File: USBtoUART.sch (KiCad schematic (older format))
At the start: 21 parts, among them J4 UJ2-MIBH-4-SMT-TR, U1 FT2232D-REEL, Y1 AS-6.000-12-2020-EXT-SMD-TR

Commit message: Changed J9 connections to help with layout.
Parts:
- JP4, JP5: footprint SMT-JUMPER_3_1-NC -> Jumpers:SMT-JUMPER_3_1-NC_TRACE_NO-SILK
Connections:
- net labels added: 3V3OUT, EEDATA, RESET, RSTOUT, USBDM, USBDM_IN, USBDP, USBDP_IN, XOUT, XTIN
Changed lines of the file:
@@
 Wire Wire Line
 	2600 1350 2750 1350
-Text HLabel 4450 3800 0    50   Input ~ 0
+Text HLabel 4150 3800 0    50   Input ~ 0
 GPS.TXD
-Text HLabel 4450 3900 0    50   Input ~ 0
+Text HLabel 4150 3900 0    50   Input ~ 0
 GPS.RXD
-Wire Wire Line
-	4450 3900 4650 3900
-Wire Wire Line
-	4450 3800 4650 3800
 Text HLabel 1400 4800 0    50   Input ~ 0
 UART2.RXD
@@
 F 0 "JP5" H 2104 4905 45  0000 L CNN
 F 1 "JUMPER-SMT_3_1-NC" H 2104 4989 45  0000 L CNN
-F 2 "SMT-JUMPER_3_1-NC" H 2000 5250 20  0001 C CNN
+F 2 "Jumpers:SMT-JUMPER_3_1-NC_TRACE_NO-SILK" H 2000 5250 20  0001 C CNN
 F 3 "" V 2000 4945 60  0001 C CNN
 F 4 "XXX-00000" H 2104 5084 60  0000 L CNN "PROD_ID"
@@
 AR Path="/5F7C6408/5F8DF40E" Ref="JP?"  Part="1"
 AR Path="/5F8460BD/5F8DF40E" Ref="JP4"  Part="1"
-F 0 "JP4" H 1854 5605 45  0000 L CNN
-F 1 "JUMPER-SMT_3_1-NC" H 1854 5689 45  0000 L CNN
-F 2 "SMT-JUMPER_3_1-NC" H 1750 5950 20  0001 C CNN
+F 0 "JP4" H 1854 5795 45  0000 L CNN
+F 1 "JUMPER-SMT_3_1-NC" H 1854 5711 45  0000 L CNN
+F 2 "Jumpers:SMT-JUMPER_3_1-NC_TRACE_NO-SILK" H 1750 5950 20  0001 C CNN
 F 3 "" V 1750 5645 60  0001 C CNN
-F 4 "XXX-00000" H 1854 5784 60  0000 L CNN "PROD_ID"
+F 4 "XXX-00000" H 1854 5616 60  0000 L CNN "PROD_ID"
 	1    1750 5700
 	-1   0    0    -1
@@
 	8500 3300 8500 3000
 Connection ~ 8500 3000
+Text Label 4350 2300 0    50   ~ 0
+EEDATA
+Text Label 4350 2100 0    50   ~ 0
+USBDM
+Text Label 4350 2000 0    50   ~ 0
+USBDP
+Wire Wire Line
+	4150 3800 4650 3800
+Wire Wire Line
+	4150 3900 4650 3900
+Text Label 4250 3800 0    50   ~ 0
+GPS.TXD
+Text Label 4250 3900 0    50   ~ 0
+GPS.RXD
+Text Label 3550 5000 0    50   ~ 0
+UART2.RXD
+Text Label 3550 5700 0    50   ~ 0
+UART2.TXD
+Text Label 5950 2800 0    50   ~ 0
+RSTOUT
+Text Label 5950 3000 0    50   ~ 0
+XOUT
+Text Label 5950 3100 0    50   ~ 0
+3V3OUT
+Text Label 3600 2600 0    50   ~ 0
+XTIN
+Text Label 4050 2400 0    50   ~ 0
+RESET
+Text Label 2350 2100 0    50   ~ 0
+USBDM_IN
+Text Label 2350 2000 0    50   ~ 0
+USBDP_IN
 $EndSCHEMATC

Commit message: Changed crystal for resonator. Board Layout.
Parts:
- removed C1, C2: 12pF, Capacitor_SMD:C_0805_2012Metric_Pad1.18x1.45mm_HandSolder, symbol Device:C
- removed Y1: AS-6.000-12-2020-EXT-SMD-TR, Crystal:Crystal_SMD_HC49-SD_HandSoldering, symbol Device:Crystal
- added R13: 1M, Resistor_SMD:R_0805_2012Metric_Pad1.20x1.40mm_HandSolder, symbol Device:R_US
- added Y1: CSTNR6M00GH5C000R0, LMS-6_Interface_Board:CSTNR_Resonator, symbol Device:Resonator
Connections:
- wire segments 95 -> 96
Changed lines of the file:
@@
 Title "USB to UART"
 Date "2020-10-17"
-Rev "5"
+Rev "6"
 Comp ""
 Comment1 ""
@@
 	1650 2000 2700 2000
 Wire Wire Line
-	3000 2000 4650 2000
+	3000 2000 3900 2000
 Wire Wire Line
 	1650 2100 3200 2100
@@
 Text HLabel 1400 5900 0    50   Input ~ 0
 UART2.TXD
-$Comp
-L Device:Crystal Y1
-U 1 1 5F86847C
-P 3350 3000
-F 0 "Y1" V 3304 3131 50  0000 L CNN
-F 1 "AS-6.000-12-2020-EXT-SMD-TR" V 3395 3131 50  0000 L CNN
-F 2 "Crystal:Crystal_SMD_HC49-SD_HandSoldering" H 3350 3000 50  0001 C CNN
-F 3 "http://www.raltron.com/wp-content/uploads/2016/10/crystal_as-smd.pdf" H 3350 3000 50  0001 C CNN
-F 4 "Raltron Electronics" V 3350 3000 50  0001 C CNN "Manufactuer"
-F 5 "AS-6.000-12-2020-EXT-SMD-TR" V 3350 3000 50  0001 C CNN "MPN"
-	1    3350 3000
-	0    1    1    0
-$EndComp
 Wire Wire Line
 	4650 2600 3350 2600
 Wire Wire Line
-	3350 2600 3350 2850
-Wire Wire Line
-	3350 3150 3350 3350
-Wire Wire Line
 	3350 6350 6600 6350
 Wire Wire Line
@@
 Wire Wire Line
 	6600 3000 5850 3000
-$Comp
-L Device:C C1
-U 1 1 5F869A1D
-P 2750 2800
-F 0 "C1" H 2865 2846 50  0000 L CNN
-F 1 "12pF" H 2865 2755 50  0000 L CNN
-F 2 "Capacitor_SMD:C_0805_2012Metric_Pad1.18x1.45mm_HandSolder" H 2750 2800 50  0001 C CNN
-F 3 "https://www.yageo.com/upload/media/product/productsearch/datasheet/mlcc/UPY-GP_NP0_16V-to-50V_18.pdf" H 2750 2800 50  0001 C CNN
-F 4 "Yageo" H 2750 2800 50  0001 C CNN "Manufacturer"
-F 5 "CC0805JRNPO9BN120" H 2750 2800 50  0001 C CNN "MPN"
-	1    2750 2800
-	1    0    0    -1
-$EndComp
-$Comp
-L Device:C C2
-U 1 1 5F86A608
-P 2750 3600
-F 0 "C2" H 2865 3646 50  0000 L CNN
-F 1 "12pF" H 2865 3555 50  0000 L CNN
-F 2 "Capacitor_SMD:C_0805_2012Metric_Pad1.18x1.45mm_HandSolder" H 2750 3600 50  0001 C CNN
-F 3 "https://www.yageo.com/upload/media/product/productsearch/datasheet/mlcc/UPY-GP_NP0_16V-to-50V_18.pdf" H 2750 3600 50  0001 C CNN
-F 4 "Yageo" H 2750 3600 50  0001 C CNN "Manufacturer"
-F 5 "CC0805JRNPO9BN120" H 2750 3600 50  0001 C CNN "MPN"
-	1    2750 3600
-	1    0    0    -1
-$EndComp
-$Comp
-L power:GND #PWR04
-U 1 1 5F86A976
-P 2750 3000
-F 0 "#PWR04" H 2750 2750 50  0001 C CNN
-F 1 "GND" H 2755 2827 50  0000 C CNN
-F 2 "" H 2750 3000 50  0001 C CNN
-F 3 "" H 2750 3000 50  0001 C CNN
-	1    2750 3000
-	1    0    0    -1
-$EndComp
-$Comp
-L power:GND #PWR05
-U 1 1 5F86AC39
-P 2750 3850
-F 0 "#PWR05" H 2750 3600 50  0001 C CNN
-F 1 "GND" H 2755 3677 50  0000 C CNN
-F 2 "" H 2750 3850 50  0001 C CNN
-F 3 "" H 2750 3850 50  0001 C CNN
-	1    2750 3850
-	1    0    0    -1
-$EndComp
-Wire Wire Line
-	2750 3850 2750 3750
-Wire Wire Line
-	2750 3450 2750 3350
-Wire Wire Line
-	2750 3350 3350 3350
-Connection ~ 3350 3350
-Wire Wire Line
-	3350 3350 3350 6350
-Wire Wire Line
-	2750 2650 2750 2600
-Wire Wire Line
-	2750 2600 3350 2600
-Connection ~ 3350 2600
-Wire Wire Line
-	2750 2950 2750 3000
 $Comp
 L power:GND #PWR010
@@
 Wire Wire Line
 	4350 2500 4650 2500
-Wire Wire Line
-	3500 2100 3900 2100
-Wire Wire Line
-	3900 1400 3900 2100
-Connection ~ 3900 2100
-Wire Wire Line
-	3900 2100 4650 2100
 Wire Wire Line
 	5650 1700 5650 1750
@@
 Text Label 2350 2000 0    50   ~ 0
 USBDP_IN
+Wire Wire Line
+	3500 2100 4650 2100
+Wire Wire Line
+	3900 1400 3900 2000
+Connection ~ 3900 2000
+Wire Wire Line
+	3900 2000 4650 2000
+$Comp
+L Device:Resonator Y1
+U 1 1 5F90F2B8
+P 3350 3100
+F 0 "Y1" V 3100 2950 50  0000 L CNN
+F 1 "CSTNR6M00GH5C000R0" H 3550 3050 50  0000 L CNN
+F 2 "LMS-6_Interface_Board:CSTNR_Resonator" H 3325 3100 50  0001 C CNN
+F 3 "http://www.murata.com/products/productdata/8801159675934/SPEC-CSTNR4M00GH5L000R0.pdf" H 3325 3100 50  0001 C CNN
+F 4 "Murata Electronics" H 3350 3100 50  0001 C CNN "Manufacaturer"
+F 5 "CSTNR6M00GH5C000R0" H 3350 3100 50  0001 C CNN "MPN"
+	1    3350 3100
+	0    1    1    0
+$EndComp
+Wire Wire Line
+	3350 3250 3350 3450
+$Comp
+L power:GND #PWR04
+U 1 1 5F9206BB
+P 2950 3200
+F 0 "#PWR04" H 2950 2950 50  0001 C CNN
+F 1 "GND" H 2955 3027 50  0000 C CNN
+F 2 "" H 2950 3200 50  0001 C CNN
+F 3 "" H 2950 3200 50  0001 C CNN
+	1    2950 3200
+	1    0    0    -1
+$EndComp
+Wire Wire Line
+	2950 3200 2950 3100
+Wire Wire Line
+	2950 3100 3150 3100
+$Comp
+L Device:R_US R13
+U 1 1 5F92454E
+P 3700 3050
+F 0 "R13" V 3495 3050 50  0000 C CNN
+F 1 "1M" V 3586 3050 50  0000 C CNN
+F 2 "Resistor_SMD:R_0805_2012Metric_Pad1.20x1.40mm_HandSolder" V 3740 3040 50  0001 C CNN
+F 3 "https://www.yageo.com/upload/media/product/productsearch/datasheet/rchip/PYu-RC_Group_51_RoHS_L_11.pdf" H 3700 3050 50  0001 C CNN
+F 4 "Yageo" V 3700 3050 50  0001 C CNN "Manufacturer"
+F 5 "RC0805FR-071ML" V 3700 3050 50  0001 C CNN "MPN"
+	1    3700 3050
+	-1   0    0    1
+$EndComp
+Wire Wire Line
+	3700 3200 3700 3450
+Wire Wire Line
+	3700 3450 3350 3450
+Connection ~ 3350 3450
+Wire Wire Line
+	3350 3450 3350 6350
+Wire Wire Line
+	3700 2900 3700 2800
+Wire Wire Line
+	3700 2800 3350 2800
+Wire Wire Line
+	3350 2600 3350 2800
+Connection ~ 3350 2800
+Wire Wire Line
+	3350 2800 3350 2950
 $EndSCHEMATC

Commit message: Fixed DRC Errors
Fixed drc errors
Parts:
- U1: footprint digikey-footprints:LQFP-48_7x7mm -> LMS-6_Interface_Board:LQFP-48_7x7mm_Narrow_Pad
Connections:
- net USBDM renamed USBD_N
- net USBDM_IN renamed IN_USBD_N
- net USBDP renamed USBD_P
- net USBDP_IN renamed IN_USBD_P
- no-connect marks 0 -> 26
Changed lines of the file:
@@
 Title "USB to UART"
 Date "2020-10-17"
-Rev "6"
+Rev "7"
 Comp ""
 Comment1 ""
@@
 F 0 "U1" H 5894 1453 60  0000 L CNN
 F 1 "FT2232D-REEL" H 5894 1347 60  0000 L CNN
-F 2 "digikey-footprints:LQFP-48_7x7mm" V 5650 2700 60  0001 L CNN
+F 2 "LMS-6_Interface_Board:LQFP-48_7x7mm_Narrow_Pad" V 5650 2700 60  0001 L CNN
 F 3 "http://www.ftdichip.com/Support/Documents/DataSheets/ICs/DS_FT2232D.pdf" H 5650 2800 60  0001 L CNN
 F 4 "768-1010-1-ND" H 5650 2900 60  0001 L CNN "Digi-Key_PN"
@@
 	1    0    0    -1
 $EndComp
-Wire Wire Line
-	1650 1900 2000 1900
 $Comp
 L Device:C C4
@@
 EEDATA
 Text Label 4350 2100 0    50   ~ 0
-USBDM
+USBD_N
 Text Label 4350 2000 0    50   ~ 0
-USBDP
+USBD_P
 Wire Wire Line
 	4150 3800 4650 3800
@@
 RESET
 Text Label 2350 2100 0    50   ~ 0
-USBDM_IN
+IN_USBD_N
 Text Label 2350 2000 0    50   ~ 0
-USBDP_IN
+IN_USBD_P
 Wire Wire Line
 	3500 2100 4650 2100
@@
 Wire Wire Line
 	3350 2800 3350 2950
+NoConn ~ 4650 2200
+NoConn ~ 4650 2700
+NoConn ~ 4650 2800
+NoConn ~ 4650 2900
+NoConn ~ 4650 3000
+NoConn ~ 4650 3100
+NoConn ~ 4650 3200
+NoConn ~ 4650 3300
+NoConn ~ 4650 3400
+NoConn ~ 4650 3500
+NoConn ~ 4650 3600
+NoConn ~ 4650 3700
+NoConn ~ 4650 4000
+NoConn ~ 4650 4100
+NoConn ~ 4650 4200
+NoConn ~ 4650 4300
+NoConn ~ 4650 4400
+NoConn ~ 4650 4500
+NoConn ~ 4650 4600
+NoConn ~ 4650 4700
+NoConn ~ 4650 4800
+NoConn ~ 4650 4900
+NoConn ~ 4650 5000
+NoConn ~ 5850 2900
+NoConn ~ 5850 2700
+NoConn ~ 1650 2200
+Wire Wire Line
+	1650 1900 2000 1900
+$Comp
+L power:PWR_FLAG #FLG0101
+U 1 1 5F9D554F
+P 4000 1550
+F 0 "#FLG0101" H 4000 1625 50  0001 C CNN
+F 1 "PWR_FLAG" H 4000 1723 50  0000 C CNN
+F 2 "" H 4000 1550 50  0001 C CNN
+F 3 "~" H 4000 1550 50  0001 C CNN
+	1    4000 1550
+	1    0    0    -1
+$EndComp
+$Comp
+L power:PWR_FLAG #FLG0102
+U 1 1 5F9D8D04
+P 5950 1750
+F 0 "#FLG0102" H 5950 1825 50  0001 C CNN
+F 1 "PWR_FLAG" V 5950 1878 50  0000 L CNN
+F 2 "" H 5950 1750 50  0001 C CNN
+F 3 "~" H 5950 1750 50  0001 C CNN
+	1    5950 1750
+	0    1    1    0
+$EndComp
+Connection ~ 5950 1750
 $EndSCHEMATC

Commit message: Fixing component field names, because I can't spell.
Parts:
- Y1: Manufacaturer Murata Electronics -> (none); Manufacturer (none) -> Murata Electronics
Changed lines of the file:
@@
 F 2 "LMS-6_Interface_Board:CSTNR_Resonator" H 3325 3100 50  0001 C CNN
 F 3 "http://www.murata.com/products/productdata/8801159675934/SPEC-CSTNR4M00GH5L000R0.pdf" H 3325 3100 50  0001 C CNN
-F 4 "Murata Electronics" H 3350 3100 50  0001 C CNN "Manufacaturer"
+F 4 "Murata Electronics" H 3350 3100 50  0001 C CNN "Manufacturer"
 F 5 "CSTNR6M00GH5C000R0" H 3350 3100 50  0001 C CNN "MPN"
 	1    3350 3100

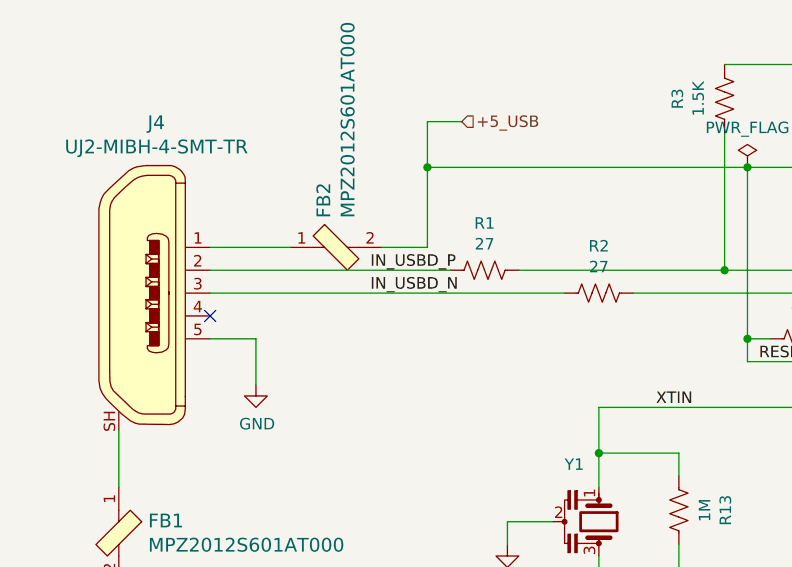
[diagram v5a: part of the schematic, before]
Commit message: Fixed USB pins
Fixed USB pin swap. Closes #7
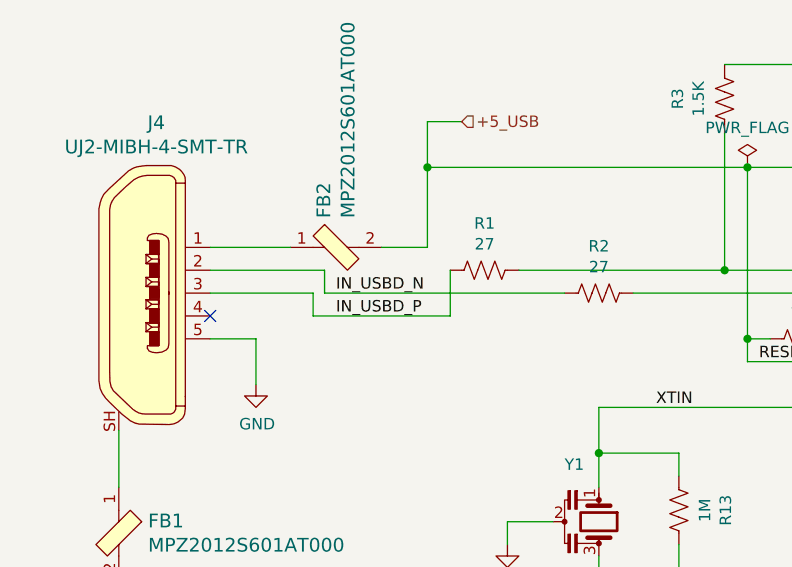
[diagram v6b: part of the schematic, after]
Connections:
- net IN_USBD_N: now also J4.2; no longer J4.3
- net IN_USBD_P: now also J4.3; no longer J4.2
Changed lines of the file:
@@
 $EndComp
-Wire Wire Line
-	1650 2000 2700 2000
 Wire Wire Line
 	3000 2000 3900 2000
-Wire Wire Line
-	1650 2100 3200 2100
 $Comp
 L Device:R_US R3
@@
 Text Label 4050 2400 0    50   ~ 0
 RESET
-Text Label 2350 2100 0    50   ~ 0
+Text Label 2200 2100 0    50   ~ 0
 IN_USBD_N
-Text Label 2350 2000 0    50   ~ 0
+Text Label 2200 2200 0    50   ~ 0
 IN_USBD_P
 Wire Wire Line
@@
 $EndComp
 Connection ~ 5950 1750
+Wire Wire Line
+	1650 2100 2100 2100
+Wire Wire Line
+	2100 2100 2100 2200
+Wire Wire Line
+	2100 2200 2700 2200
+Wire Wire Line
+	2700 2200 2700 2000
+Wire Wire Line
+	1650 2000 2150 2000
+Wire Wire Line
+	2150 2000 2150 2100
+Wire Wire Line
+	2150 2100 3200 2100
 $EndSCHEMATC

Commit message: Rev C Board layout
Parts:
- D2: footprint digikey-footprints:0805 -> LED_SMD:LED_0805_2012Metric_Pad1.15x1.40mm_HandSolder
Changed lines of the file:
@@
 F 0 "D2" H 7750 3037 60  0000 C CNN
 F 1 "LG R971-KN-1" H 7750 2931 60  0000 C CNN
-F 2 "digikey-footprints:0805" H 8000 2900 60  0001 L CNN
+F 2 "LED_SMD:LED_0805_2012Metric_Pad1.15x1.40mm_HandSolder" H 8000 2900 60  0001 L CNN
 F 3 "https://dammedia.osram.info/media/resource/hires/osram-dam-2493888/LH%20R974.pdf" H 8000 3000 60  0001 L CNN
 F 4 "475-1410-1-ND" H 8000 3100 60  0001 L CNN "Digi-Key_PN"
